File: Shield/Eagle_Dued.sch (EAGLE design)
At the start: 48 parts, among them IC1 7805TV, IC2 LM340MP-05

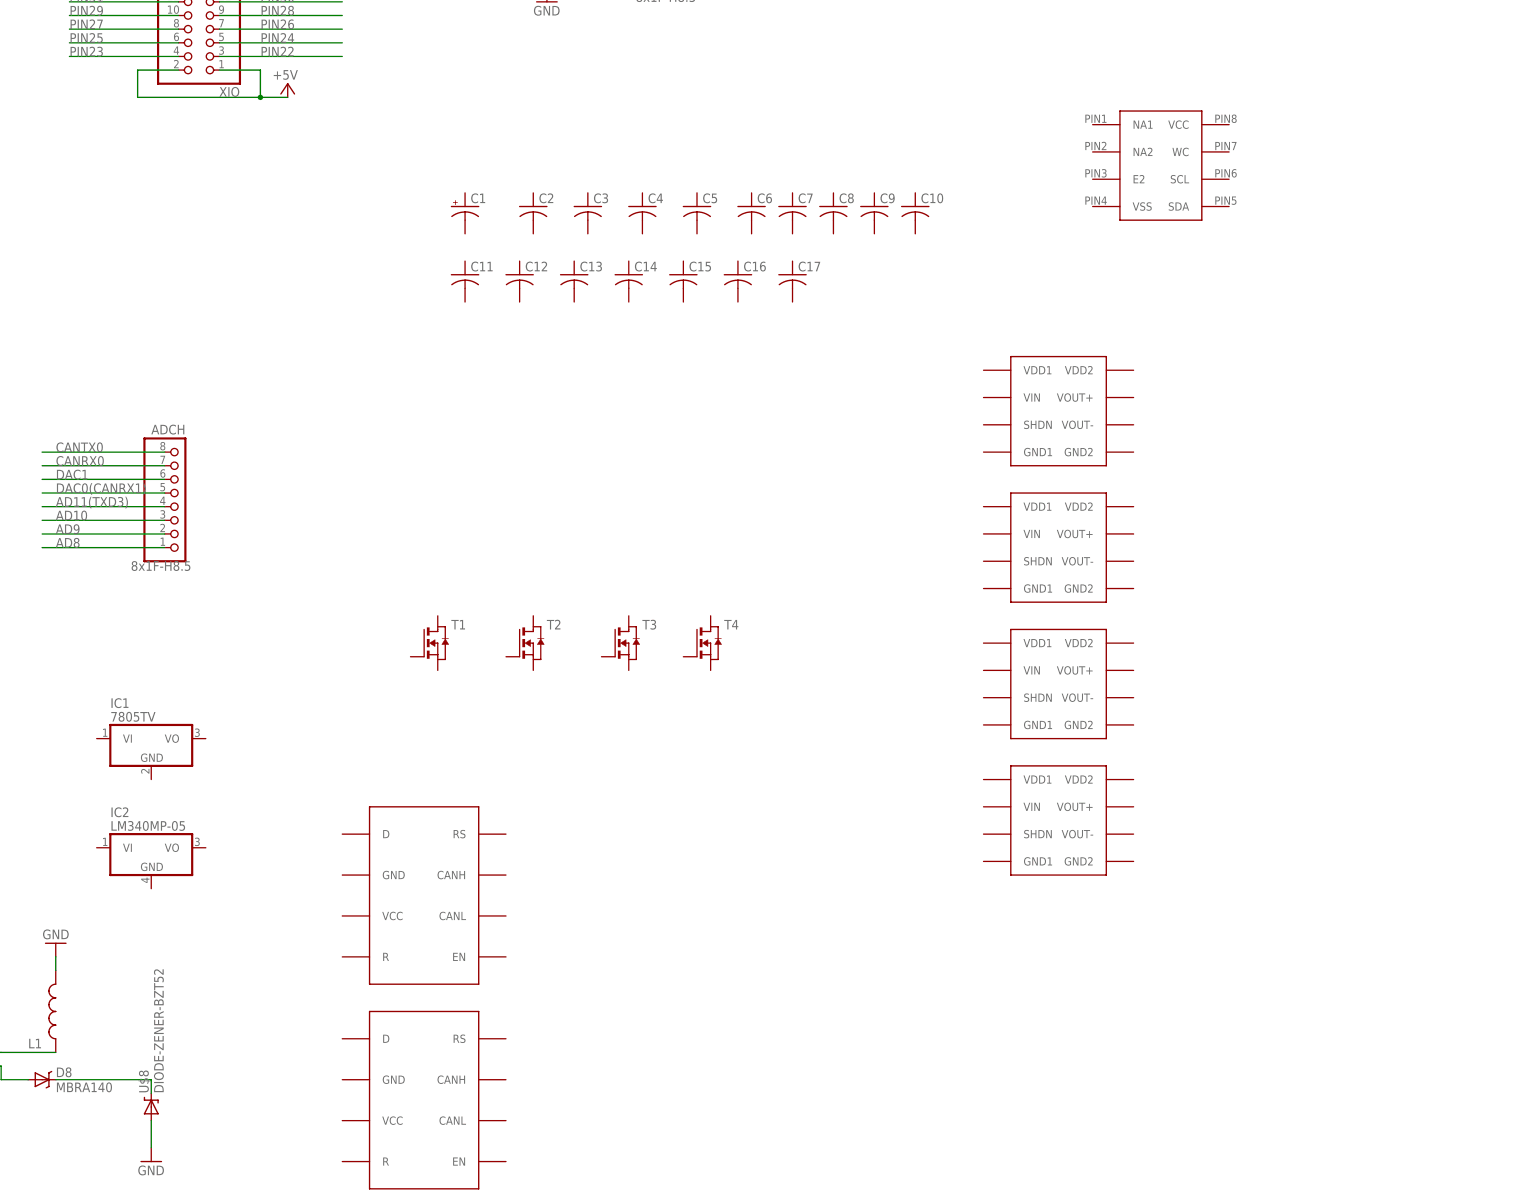
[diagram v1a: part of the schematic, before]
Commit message: Implemented power section of schematic for shield.
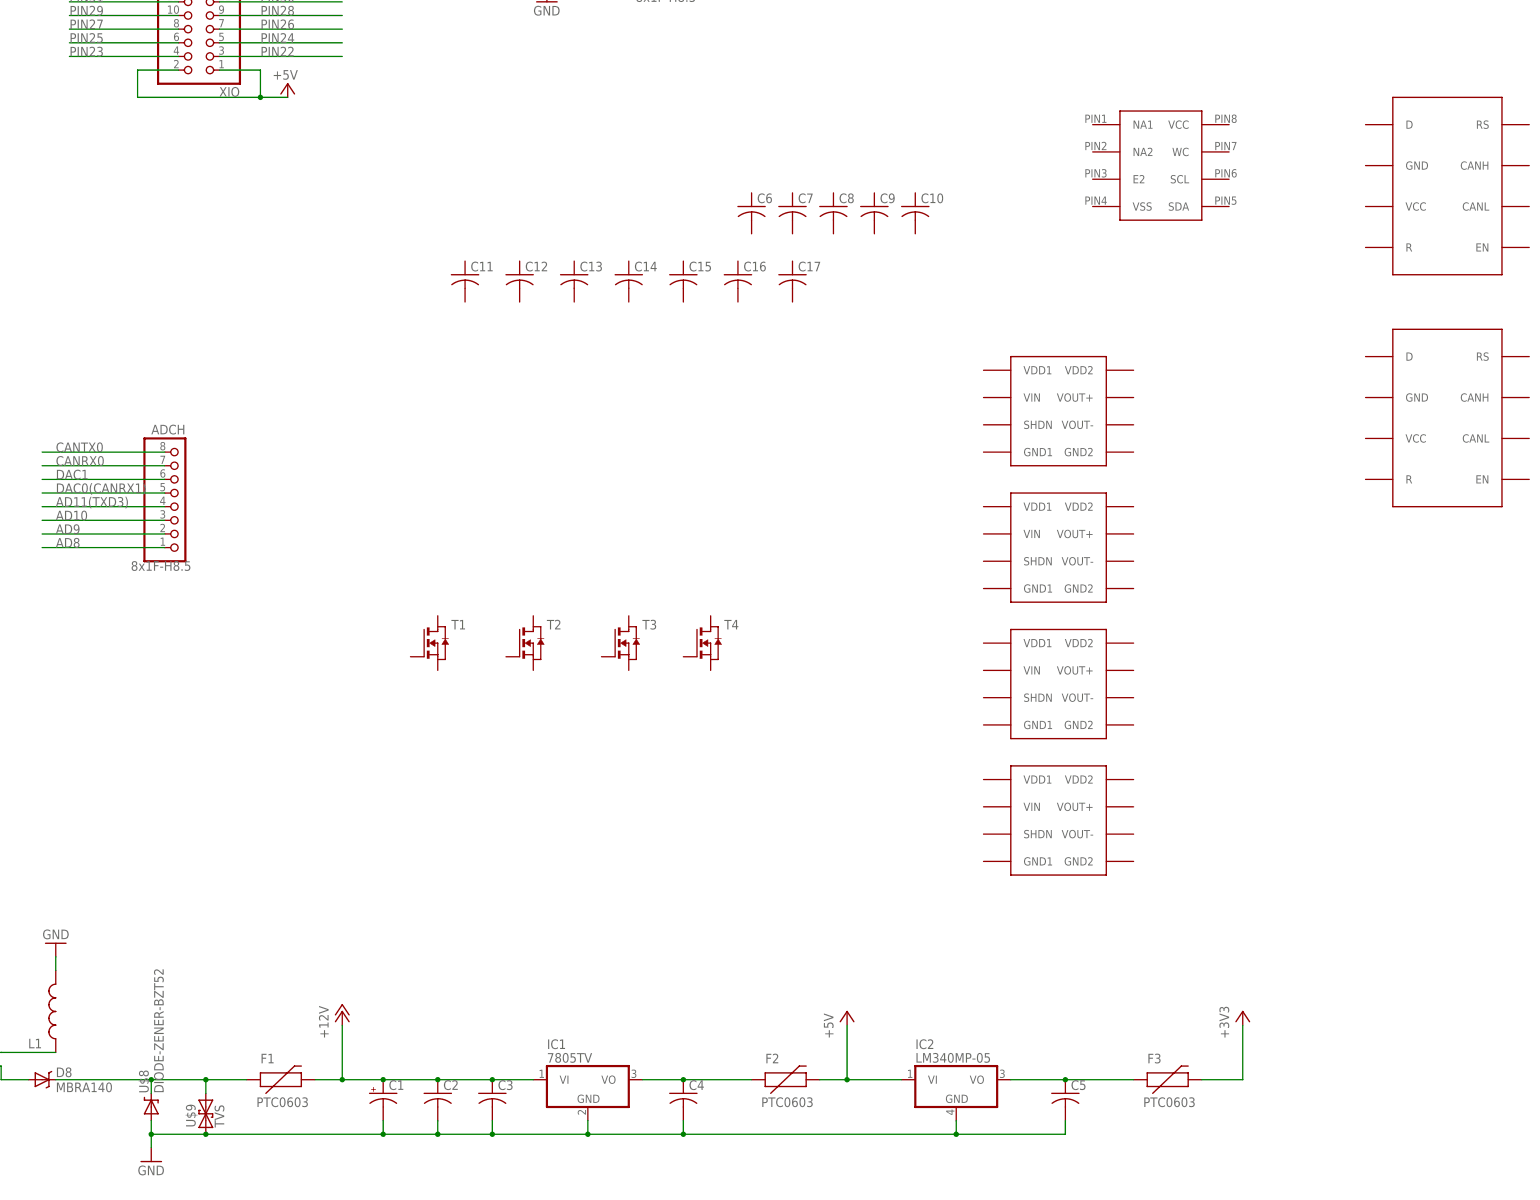
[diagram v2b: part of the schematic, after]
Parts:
- added F1, F2, F3: PTC0603, SparkFun-PowerIC:PTC0603
- added U$9: TVS, SparkFun-DiscreteSemi:TVS
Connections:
- new net +12V: C1.+, C2.1, C3.1, F1.2, IC1.VI
- new net N$6: C4.1, F2.1, IC1.VO
- new net N$8: C5.1, F3.1, IC2.VO
- net +3V3: now also F3.2
- net +5V: now also F2.2, IC2.VI
- net GND: now also C1.-, C2.2, C3.2, C4.2, C5.2, IC1.GND, IC2.GND, U$9.1
- net N$3: now also F1.1, U$9.2
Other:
- moved on the sheet: C1, C2, C3, C4, C5, IC1, IC2
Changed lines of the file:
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@@
 <part name="U$8" library="SparkFun-DiscreteSemi" deviceset="DIODE-ZENER" device="-BZT52"/>
 <part name="GND2" library="supply1" deviceset="GND" device=""/>
+<part name="U$9" library="SparkFun-DiscreteSemi" deviceset="TVS" device=""/>
+<part name="F1" library="SparkFun-PowerIC" deviceset="PTC" device="0603"/>
+<part name="F2" library="SparkFun-PowerIC" deviceset="PTC" device="0603"/>
+<part name="F3" library="SparkFun-PowerIC" deviceset="PTC" device="0603"/>
+<part name="P+1" library="supply1" deviceset="+12V" device=""/>
+<part name="P+2" library="supply1" deviceset="+5V" device=""/>
+<part name="+3V1" library="supply1" deviceset="+3V3" device=""/>
 </parts>
 <sheets>
@@
 <instance part="T3" gate="A" x="444.5" y="50.8"/>
 <instance part="T4" gate="A" x="459.74" y="50.8"/>
-<instance part="C1" gate="G$1" x="414.02" y="132.08"/>
-<instance part="C2" gate="G$1" x="426.72" y="132.08"/>
-<instance part="C3" gate="G$1" x="436.88" y="132.08"/>
-<instance part="C4" gate="G$1" x="447.04" y="132.08"/>
-<instance part="C5" gate="G$1" x="457.2" y="132.08"/>
+<instance part="C1" gate="G$1" x="398.78" y="-33.02"/>
+<instance part="C2" gate="G$1" x="408.94" y="-33.02"/>
+<instance part="C3" gate="G$1" x="419.1" y="-33.02"/>
+<instance part="C4" gate="G$1" x="454.66" y="-33.02"/>
+<instance part="C5" gate="G$1" x="525.78" y="-33.02"/>
 <instance part="C6" gate="G$1" x="467.36" y="132.08"/>
 <instance part="C7" gate="G$1" x="474.98" y="132.08"/>
@@
 <instance part="U$4" gate="G$1" x="515.62" y="7.62"/>
 <instance part="U$5" gate="G$1" x="535.94" y="129.54"/>
-<instance part="U$6" gate="G$1" x="396.24" y="-12.7"/>
-<instance part="U$7" gate="G$1" x="396.24" y="-50.8"/>
-<instance part="IC1" gate="A1" x="355.6" y="33.02"/>
-<instance part="IC2" gate="A" x="355.6" y="12.7"/>
+<instance part="U$6" gate="G$1" x="586.74" y="119.38"/>
+<instance part="U$7" gate="G$1" x="586.74" y="76.2"/>
+<instance part="IC1" gate="A1" x="436.88" y="-30.48"/>
+<instance part="IC2" gate="A" x="505.46" y="-30.48"/>
 <instance part="L1" gate="G$1" x="337.82" y="-17.78" rot="R180"/>
 <instance part="JP1" gate="G$1" x="307.34" y="-25.4"/>
@@
 <instance part="U$8" gate="G$1" x="355.6" y="-35.56" rot="R90"/>
 <instance part="GND2" gate="1" x="355.6" y="-45.72"/>
+<instance part="U$9" gate="G$1" x="365.76" y="-38.1" rot="R90"/>
+<instance part="F1" gate="G$1" x="378.46" y="-30.48"/>
+<instance part="F2" gate="G$1" x="472.44" y="-30.48"/>
+<instance part="F3" gate="G$1" x="543.56" y="-30.48"/>
+<instance part="P+1" gate="1" x="391.16" y="-17.78"/>
+<instance part="P+2" gate="1" x="485.14" y="-17.78"/>
+<instance part="+3V1" gate="G$1" x="558.8" y="-17.78"/>
 </instances>
 <busses>
@@
 <pinref part="P+12" gate="1" pin="+5V"/>
 </segment>
+<segment>
+<pinref part="F2" gate="G$1" pin="2"/>
+<wire x1="480.06" y1="-30.48" x2="485.14" y2="-30.48" width="0.1524" layer="91"/>
+<pinref part="IC2" gate="A" pin="VI"/>
+<pinref part="P+2" gate="1" pin="+5V"/>
+<wire x1="485.14" y1="-30.48" x2="495.3" y2="-30.48" width="0.1524" layer="91"/>
+<wire x1="485.14" y1="-20.32" x2="485.14" y2="-30.48" width="0.1524" layer="91"/>
+<junction x="485.14" y="-30.48"/>
+</segment>
 </net>
 <net name="GND" class="0">
@@
 <pinref part="U$8" gate="G$1" pin="A"/>
 <pinref part="GND2" gate="1" pin="GND"/>
-<wire x1="355.6" y1="-38.1" x2="355.6" y2="-43.18" width="0.1524" layer="91"/>
+<wire x1="355.6" y1="-38.1" x2="355.6" y2="-40.64" width="0.1524" layer="91"/>
+<pinref part="U$9" gate="G$1" pin="1"/>
+<wire x1="355.6" y1="-40.64" x2="355.6" y2="-43.18" width="0.1524" layer="91"/>
+<wire x1="365.76" y1="-40.64" x2="355.6" y2="-40.64" width="0.1524" layer="91"/>
+<junction x="355.6" y="-40.64"/>
+<pinref part="C1" gate="G$1" pin="-"/>
+<wire x1="398.78" y1="-38.1" x2="398.78" y2="-40.64" width="0.1524" layer="91"/>
+<wire x1="398.78" y1="-40.64" x2="365.76" y2="-40.64" width="0.1524" layer="91"/>
+<junction x="365.76" y="-40.64"/>
+<pinref part="C2" gate="G$1" pin="2"/>
+<wire x1="398.78" y1="-40.64" x2="408.94" y2="-40.64" width="0.1524" layer="91"/>
+<wire x1="408.94" y1="-40.64" x2="408.94" y2="-38.1" width="0.1524" layer="91"/>
+<junction x="398.78" y="-40.64"/>
+<pinref part="C3" gate="G$1" pin="2"/>
+<wire x1="408.94" y1="-40.64" x2="419.1" y2="-40.64" width="0.1524" layer="91"/>
+<wire x1="419.1" y1="-40.64" x2="419.1" y2="-38.1" width="0.1524" layer="91"/>
+<junction x="408.94" y="-40.64"/>
+<pinref part="IC1" gate="A1" pin="GND"/>
+<wire x1="436.88" y1="-38.1" x2="436.88" y2="-40.64" width="0.1524" layer="91"/>
+<wire x1="436.88" y1="-40.64" x2="419.1" y2="-40.64" width="0.1524" layer="91"/>
+<junction x="419.1" y="-40.64"/>
+<pinref part="C4" gate="G$1" pin="2"/>
+<wire x1="454.66" y1="-38.1" x2="454.66" y2="-40.64" width="0.1524" layer="91"/>
+<wire x1="454.66" y1="-40.64" x2="436.88" y2="-40.64" width="0.1524" layer="91"/>
+<junction x="436.88" y="-40.64"/>
+<pinref part="IC2" gate="A" pin="GND"/>
+<wire x1="505.46" y1="-38.1" x2="505.46" y2="-40.64" width="0.1524" layer="91"/>
+<wire x1="505.46" y1="-40.64" x2="454.66" y2="-40.64" width="0.1524" layer="91"/>
+<junction x="454.66" y="-40.64"/>
+<pinref part="C5" gate="G$1" pin="2"/>
+<wire x1="525.78" y1="-38.1" x2="525.78" y2="-40.64" width="0.1524" layer="91"/>
+<wire x1="525.78" y1="-40.64" x2="505.46" y2="-40.64" width="0.1524" layer="91"/>
+<junction x="505.46" y="-40.64"/>
 </segment>
 </net>
@@
 <pinref part="POWER" gate="A" pin="2"/>
 </segment>
+<segment>
+<pinref part="F3" gate="G$1" pin="2"/>
+<pinref part="+3V1" gate="G$1" pin="+3V3"/>
+<wire x1="551.18" y1="-30.48" x2="558.8" y2="-30.48" width="0.1524" layer="91"/>
+<wire x1="558.8" y1="-30.48" x2="558.8" y2="-20.32" width="0.1524" layer="91"/>
+</segment>
 </net>
 <net name="PIN51" class="0">
@@
 <pinref part="U$8" gate="G$1" pin="C"/>
 <wire x1="355.6" y1="-30.48" x2="355.6" y2="-33.02" width="0.1524" layer="91"/>
-</segment>
-</net>
+<pinref part="U$9" gate="G$1" pin="2"/>
+<wire x1="355.6" y1="-30.48" x2="365.76" y2="-30.48" width="0.1524" layer="91"/>
+<wire x1="365.76" y1="-30.48" x2="365.76" y2="-33.02" width="0.1524" layer="91"/>
+<junction x="355.6" y="-30.48"/>
+<pinref part="F1" gate="G$1" pin="1"/>
+<wire x1="373.38" y1="-30.48" x2="365.76" y2="-30.48" width="0.1524" layer="91"/>
+<junction x="365.76" y="-30.48"/>
+</segment>
+</net>
+<net name="N$6" class="0">
+<segment>
+<pinref part="IC1" gate="A1" pin="VO"/>
+<pinref part="C4" gate="G$1" pin="1"/>
+<wire x1="447.04" y1="-30.48" x2="454.66" y2="-30.48" width="0.1524" layer="91"/>
+<pinref part="F2" gate="G$1" pin="1"/>
+<wire x1="454.66" y1="-30.48" x2="467.36" y2="-30.48" width="0.1524" layer="91"/>
+<junction x="454.66" y="-30.48"/>
+</segment>
+</net>
+<net name="N$8" class="0">
+<segment>
+<pinref part="C5" gate="G$1" pin="1"/>
+<pinref part="IC2" gate="A" pin="VO"/>
+<wire x1="525.78" y1="-30.48" x2="515.62" y2="-30.48" width="0.1524" layer="91"/>
+<pinref part="F3" gate="G$1" pin="1"/>
+<wire x1="525.78" y1="-30.48" x2="538.48" y2="-30.48" width="0.1524" layer="91"/>
+<junction x="525.78" y="-30.48"/>
+</segment>
+</net>
+<net name="+12V" class="0">
+<segment>
+<pinref part="F1" gate="G$1" pin="2"/>
+<pinref part="C1" gate="G$1" pin="+"/>
+<wire x1="386.08" y1="-30.48" x2="391.16" y2="-30.48" width="0.1524" layer="91"/>
+<pinref part="C2" gate="G$1" pin="1"/>
+<wire x1="391.16" y1="-30.48" x2="398.78" y2="-30.48" width="0.1524" layer="91"/>
+<wire x1="398.78" y1="-30.48" x2="408.94" y2="-30.48" width="0.1524" layer="91"/>
+<junction x="398.78" y="-30.48"/>
+<pinref part="C3" gate="G$1" pin="1"/>
+<wire x1="408.94" y1="-30.48" x2="419.1" y2="-30.48" width="0.1524" layer="91"/>
+<junction x="408.94" y="-30.48"/>
+<pinref part="IC1" gate="A1" pin="VI"/>
+<wire x1="419.1" y1="-30.48" x2="426.72" y2="-30.48" width="0.1524" layer="91"/>
+<junction x="419.1" y="-30.48"/>
+<pinref part="P+1" gate="1" pin="+12V"/>
+<wire x1="391.16" y1="-20.32" x2="391.16" y2="-30.48" width="0.1524" layer="91"/>
+<junction x="391.16" y="-30.48"/>
+</segment>
+</net>

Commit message: Schematic of DueD basically complete now.
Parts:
- removed C10, C11, C12, C13, C14, C15, C16, C17: (no value), rcl:C-USC0603
- removed U$3, U$4: ACPL-C87A-000E, ck_custom:ACPL-C87A-000E
- removed U$7: SN65HVD234, ck_custom:SN65HVD234
- added C18, C19, C21, C22, C24, C25, C27, C29: .1uF, rcl:C-USC0603
- added C20, C23, C26: 100pf, rcl:C-USC0603
- added C28, C30: 47nF, rcl:C-USC0603
- added D10, D11, D12, D9: TVS, SparkFun-DiscreteSemi:DIODESOD
- added J10: Analog Inputs, SparkFun-Connectors:M05PTH
- added J11: MOSFET OUTPUTS, SparkFun-Connectors:M05PTH
- added J12: CANBUS, SparkFun-Connectors:M04PTH
- added J8: DIGITAL INPUTS, SparkFun-Connectors:M05PTH
- added JP2: (no value), jumper:JP1E
- added OK1, OK2: ILD213, optocoupler:ILD213
- added R1, R10, R11, R13, R14, R15, R19, R2, R21, R25, R26, R27, R28, R3, R31, R37, R38, R39, R5, R6, R7, R9: 10K, rcl:R-US_R0603
- added R12, R16, R4, R8: 16K, rcl:R-US_R0603
- added R17: 510, rcl:R-US_R0603
- added R18: 330, rcl:R-US_R0603
- added R20, R22: 120, rcl:R-US_R0603
- added R23, R24: 4.7K, rcl:R-US_R0603
- added R29, R30, R32, R33, R34, R35, R36, R40: 1K, rcl:R-US_R0603
- added R41: 33, rcl:R-US_R0603
- added SJ1, SJ2, SJ3, SJ4: SOLDERJUMPERNO, SparkFun-Passives:SOLDERJUMPERNO
- added U$10, U$11, U$12: ACPL-C87A-000E, ck_custom:ACPL-C87A-000E
- added X1: 87758-1216, con-molex:87758-1216
- C1: value (none) -> 100uF
- C2: value (none) -> 1uF
- C3, C6, C7: value (none) -> .1uF
- C4: value (none) -> .33uF
- C5: value (none) -> 10uF
- C8: value (none) -> 100pf
- D2, D3, D7: value MBR0520LT -> GREEN; device diode:MBR0520LT -> SparkFun-LED:LED-GREEN0603
- U$2: value ACPL-C87A-000E -> SN65HVD234; device ck_custom:ACPL-C87A-000E -> ck_custom:SN65HVD234
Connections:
- removed net AD11(TXD3): ADCH.4
- removed net AD14(RXD3): XIO.33
- removed net AD8: ADCH.1
- removed net CANTX1/IO: XIO.34
- removed net DAC0(CANRX1): ADCH.5
- removed net PIN22: XIO.3
- removed net PIN32: XIO.13
- removed net PIN48: XIO.29
- removed net RXD0: COMMUNICATION.2
- removed net SCL0-3: COMMUNICATION.8
- removed net SDA0-3: COMMUNICATION.7
- removed net TXD0: COMMUNICATION.1
- new net AIN1: D9.C, J10.1
- new net AIN2: D10.C, J10.2
- new net AIN3: D11.C, J10.3
- new net AIN4: D12.C, J10.4
- new net CAN0-EN: ADCH.1, U$6.EN
- new net CAN1-EN: ADCH.4, U$2.EN
- new net CANH0: J12.3, SJ1.1, U$6.CANH
- new net CANH1: J12.2, SJ3.1, U$2.CANH
- new net CANL0: J12.4, SJ2.1, U$6.CANL
- new net CANL1: J12.1, SJ4.1, U$2.CANL
- new net CANRX1: ADCH.5, U$2.R
- new net CANTX1: U$2.D, XIO.34
- new net DIG1: PWMH.2, R30.2, R31.1
- new net DIG2: PWMH.4, R34.2, R37.1
- new net DIG3: PWMH.5, R39.1, R40.2
- new net DIG4: PWMH.6, R35.2, R38.1
- new net DIGOUT1: R25.1, T1.G, XIO.33
- new net DIGOUT2: R26.1, T2.G, XIO.3
- new net DIGOUT3: R27.1, T3.G, XIO.29
- new net DIGOUT4: R28.1, T4.G, XIO.13
- new net DIN1: J8.1, R29.1
- new net DIN2: J8.2, R33.1
- new net DIN3: J8.3, R32.1
- new net DIN4: J8.4, R36.1
- new net MOSFET1: D1.C, J11.2, T1.D
- new net MOSFET2: D4.C, J11.3, T2.D
- new net MOSFET3: D5.C, J11.4, T3.D
- new net MOSFET4: D6.C, J11.5, T4.D
- new net N$10: R3.2, R4.1, U$1.VIN
- new net N$11: R7.2, R8.1, U$10.VIN
- new net N$12: R5.1, U$10.VOUT+
- new net N$13: R6.1, U$10.VOUT-
- new net N$14: C20.1, R8.2
- new net N$15: R11.2, R12.1, U$11.VIN
- new net N$16: R9.1, U$11.VOUT+
- new net N$17: R10.1, U$11.VOUT-
- new net N$18: C23.1, R12.2
- new net N$19: R15.2, R16.1, U$12.VIN
- new net N$20: R13.1, U$12.VOUT+
- new net N$21: R14.1, U$12.VOUT-
- new net N$22: C26.1, R16.2
- new net N$23: D2.A, R17.2
- new net N$24: R19.2, U$6.RS
- new net N$25: D3.A, R18.2
- new net N$26: C28.1, R20.1, SJ2.2
- new net N$27: R20.2, SJ1.2
- new net N$28: R21.2, U$2.RS
- new net N$29: C30.1, R22.1, SJ4.2
- new net N$30: R22.2, SJ3.2
- new net N$31: OK1A.A, R29.2
- new net N$32: OK1B.A, R33.2
- new net N$33: OK1A.COL, R30.1
- new net N$34: OK1B.COL, R34.1
- new net N$35: X1-5.S, X1-7.S
- new net N$36: OK2B.COL, R35.1
- new net N$37: D7.A, R41.1
- new net N$38: OK2A.COL, R40.1
- new net N$39: R41.2, X1-12.S
- new net N$4: JP1.3, JP2.1
- new net N$40: OK2A.A, R32.2
- new net N$43: OK2B.A, R36.2
- new net N$5: R1.1, U$1.VOUT+
- new net N$7: R2.1, U$1.VOUT-
- new net N$9: C8.1, R4.2
- new net RXD3: COMMUNICATION.7, X1-4.S
- new net SCL: COMMUNICATION.1, R23.2, U$5.SCL
- new net SDA: COMMUNICATION.2, R24.2, U$5.SDA
- new net TXD3: COMMUNICATION.8, X1-3.S
- net +3V3: now also C27.1, C29.1, C9.1, R18.1, R23.1, R24.1, R31.2, R37.2, R38.2, R39.2, U$2.VCC, U$5.VCC, U$6.VCC, X1-1.S
- net +5V: now also C18.1, C19.1, C21.1, C22.1, C24.1, C25.1, C6.1, C7.1, JP1.4, R17.1, U$1.VDD1, U$1.VDD2, U$10.VDD1, U$10.VDD2, U$11.VDD1, U$11.VDD2, U$12.VDD1, U$12.VDD2
- net AD0: now also R1.2
- net AD1: now also R2.2
- net AD2: now also R5.2
- net AD3: now also R6.2
- net AD4: now also R9.2
- net AD5: now also R10.2
- net AD6: now also R13.2
- net AD7: now also R14.2
- net CANRX0: now also U$6.R
- net CANTX0: now also U$6.D
- net GND: now also C18.2, C19.2, C20.2, C21.2, C22.2, C23.2, C24.2, C25.2, C26.2, C27.2, C28.2, C29.2, C30.2, C6.2, C7.2, C8.2, C9.2, D1.A, D10.A, D11.A, D12.A, D2.C, D3.C, D4.A, D5.A, D6.A, D7.C, D9.A, J10.5, J11.1, J8.5, OK1A.C, OK1A.EMIT, OK1B.C, OK1B.EMIT, OK2A.C, OK2A.EMIT, OK2B.C, OK2B.EMIT, R11.1, R15.1, R19.1, R21.1, R25.2, R26.2, R27.2, R28.2, R3.1, R7.1, T1.S, T2.S, T3.S, T4.S, U$1.GND1, U$1.GND2, U$1.SHDN, U$10.GND1, U$10.GND2, U$10.SHDN, U$11.GND1, U$11.GND2, U$11.SHDN, U$12.GND1, U$12.GND2, U$12.SHDN, U$2.GND, U$5.E2, U$5.NA1, U$5.NA2, U$5.VSS, U$6.GND, X1-2.S
- net RXD1: now also U$5.WC
- net RXD2: now also X1-10.S
- net VIN: now also JP2.2
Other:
- note added: "ANALOG INPUTS"
- note added: "CANBUS"
- note added: "DIGITAL INPUT"
- note added: "EEPROM STORAGE"
- note added: "MOSFET OUTPUTS"
- moved on the sheet: C6, C7, C8, C9, D1, D4, D5, D6, T1, T2, T3, T4
